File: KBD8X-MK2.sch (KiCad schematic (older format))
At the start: 22 parts, among them J1 AVR-ISP-6, Q1 DSS60601MZ4-13, SW1 SW_Push, U1 ATmega32U4-MU, U2 PRTR5V0U2X, Y1 16MHz

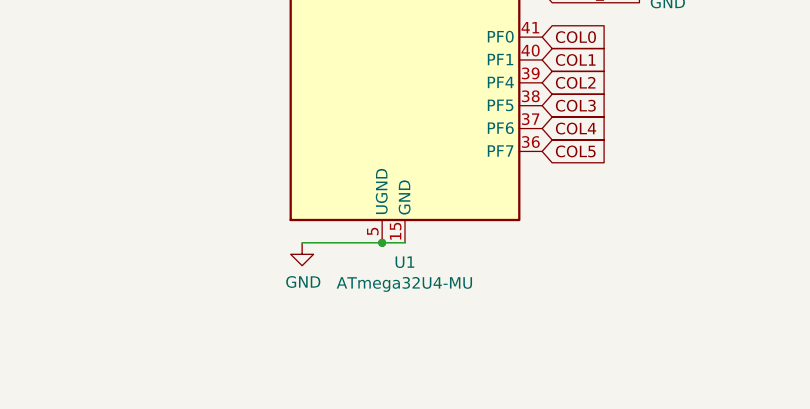
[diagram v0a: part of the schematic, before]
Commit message: Fix PCB footprint mistake
There was a mistake with one of the footprints, which was not changed. All footprints are now Alps-compatible and the Gerber files have been updated.
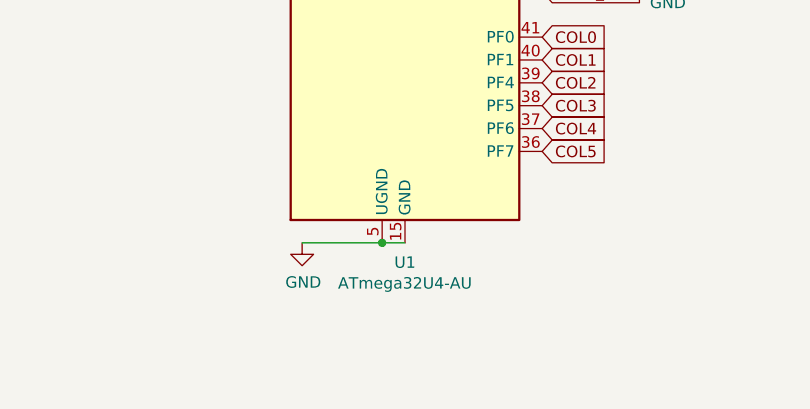
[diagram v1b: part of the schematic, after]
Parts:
- U1: value ATmega32U4-MU -> ATmega32U4-AU; footprint locallib:QFN-44-1EP_7x7mm_Pitch0.5mm -> Package_QFP:TQFP-44_10x10mm_P0.8mm
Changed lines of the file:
@@
 P 4800 5050
 F 0 "U1" H 4800 3164 50  0000 C CNN
-F 1 "ATmega32U4-MU" H 4800 3073 50  0000 C CNN
-F 2 "locallib:QFN-44-1EP_7x7mm_Pitch0.5mm" H 4800 5050 50  0001 C CIN
+F 1 "ATmega32U4-AU" H 4800 3073 50  0000 C CNN
+F 2 "Package_QFP:TQFP-44_10x10mm_P0.8mm" H 4800 5050 50  0001 C CIN
 F 3 "http://ww1.microchip.com/downloads/en/DeviceDoc/Atmel-7766-8-bit-AVR-ATmega16U4-32U4_Datasheet.pdf" H 4800 5050 50  0001 C CNN
 	1    4800 5050
